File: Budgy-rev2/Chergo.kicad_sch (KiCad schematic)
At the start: 36 parts, among them K1 KEYSW, K10 KEYSW, K11 KEYSW, K12 KEYSW, K13 KEYSW, K14 KEYSW, K15 KEYSW, K16 KEYSW, K17 KEYSW, K2 KEYSW, K3 KEYSW, K4 KEYSW, K5 KEYSW, K6 KEYSW, K7 KEYSW, K8 KEYSW, K9 KEYSW, U1 Pico, U2 TRRS

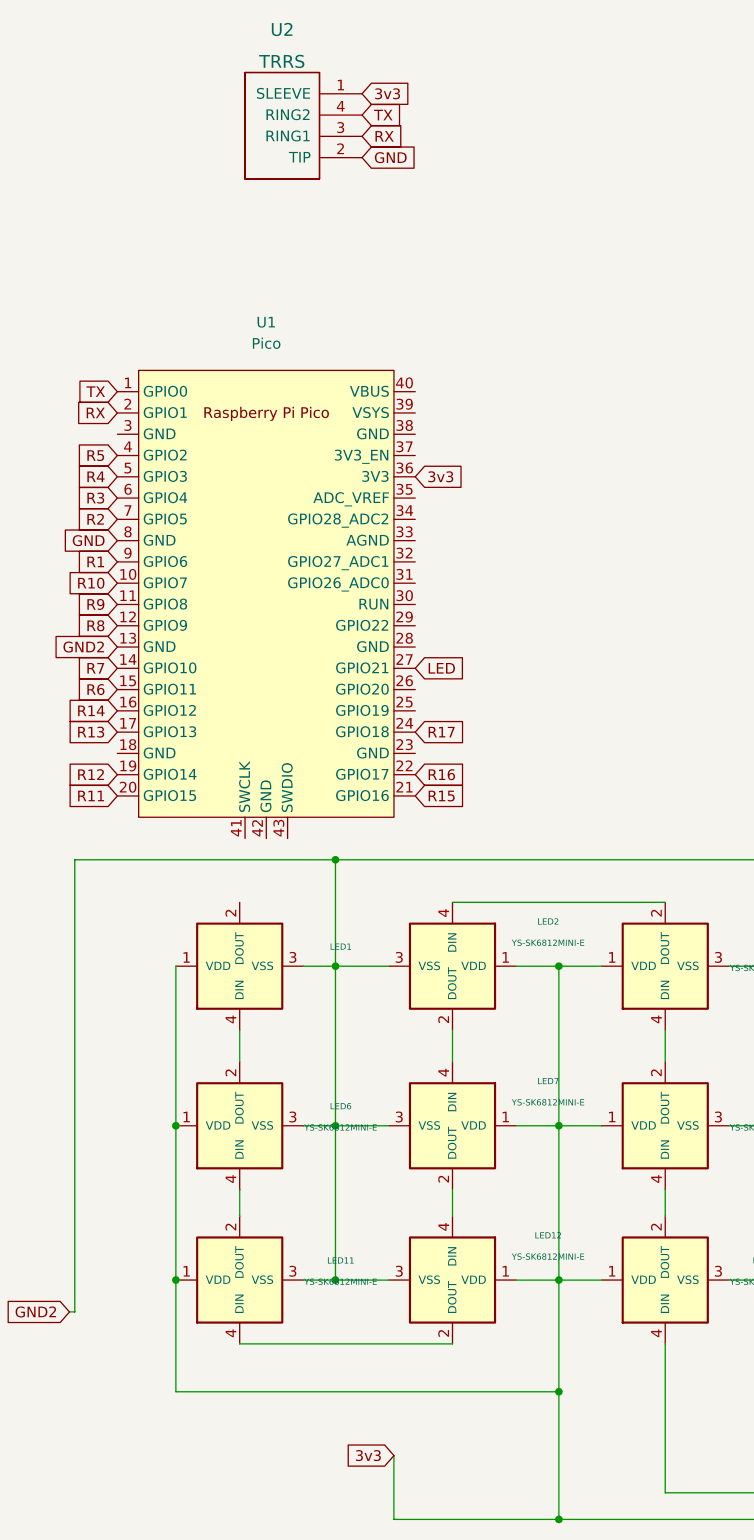
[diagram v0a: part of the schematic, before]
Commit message: changed to 5v for rgbled
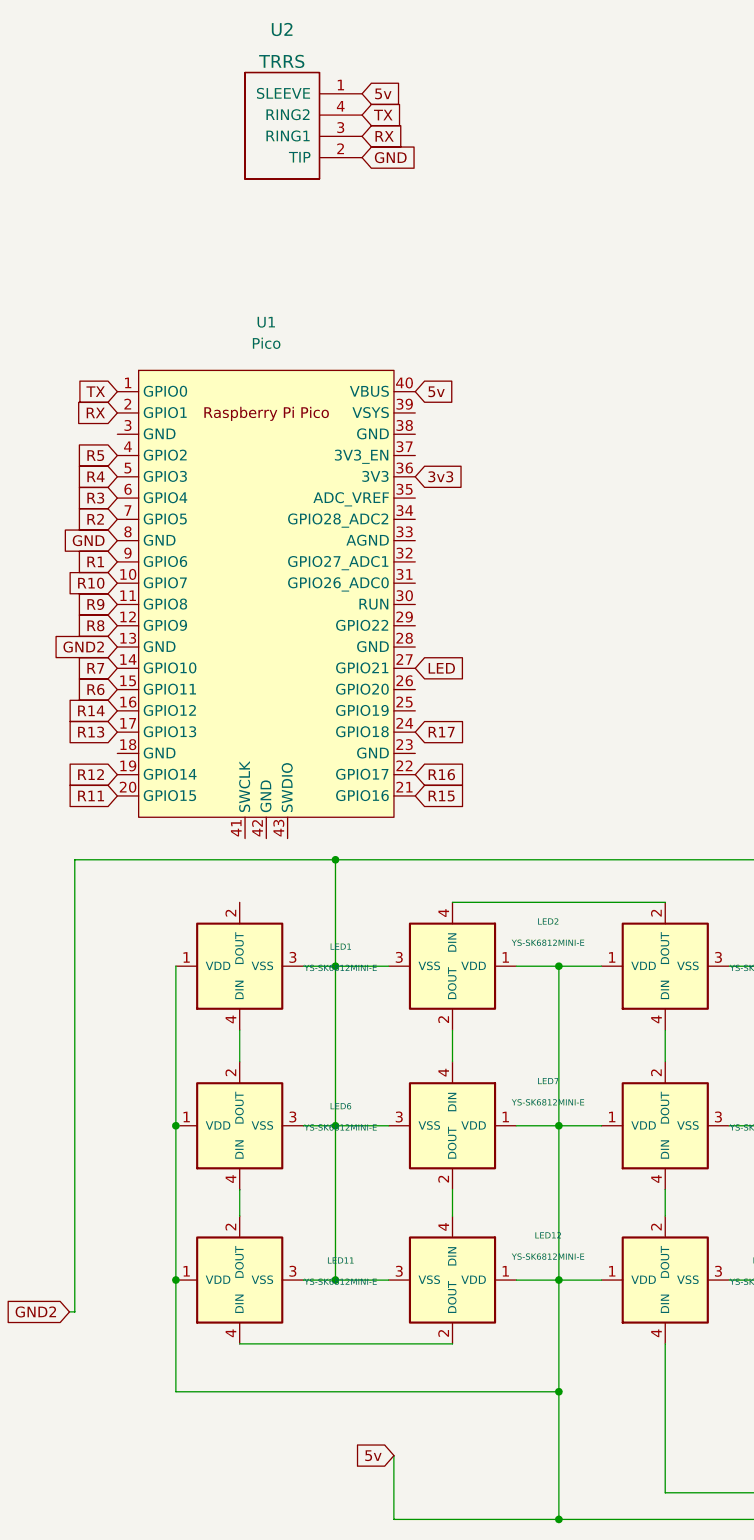
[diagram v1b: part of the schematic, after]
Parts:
- LED1: value (none) -> YS-SK6812MINI-E; footprint (none) -> kbd:YS-SK6812MINI-E-reversible-fix
- LED10, LED11, LED12, LED13, LED14, LED15, LED16, LED17, LED2, LED3, LED4, LED5, LED6, LED7, LED8, LED9: footprint (none) -> kbd:YS-SK6812MINI-E-reversible-fix
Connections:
- net 3v3: no longer LED1.1 (VDD), LED10.1 (VDD), LED11.1 (VDD), LED12.1 (VDD), LED13.1 (VDD), LED14.1 (VDD), LED15.1 (VDD), LED16.1 (VDD), LED17.1 (VDD), LED2.1 (VDD), LED3.1 (VDD), LED4.1 (VDD), LED5.1 (VDD), LED6.1 (VDD), LED7.1 (VDD), LED8.1 (VDD), LED9.1 (VDD), U2.1 (SLEEVE)
- net 5v: now reaches U1.40 (VBUS)
- net 5v: now also LED1.1 (VDD), LED10.1 (VDD), LED11.1 (VDD), LED12.1 (VDD), LED13.1 (VDD), LED14.1 (VDD), LED15.1 (VDD), LED16.1 (VDD), LED17.1 (VDD), LED2.1 (VDD), LED3.1 (VDD), LED4.1 (VDD), LED5.1 (VDD), LED6.1 (VDD), LED7.1 (VDD), LED8.1 (VDD), LED9.1 (VDD), U2.1 (SLEEVE)
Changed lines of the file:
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@@
     (stroke (width 0) (type default) (color 0 0 0 0))
   )
-  (global_label "3v3" (shape input) (at 55.245 23.495 0) (fields_autoplaced)
-    (effects (font (size 1.27 1.27)) (justify left))
-    (property "Intersheet References" "${INTERSHEET_REFS}" (id 0) (at 61.0448 23.4156 0)
-      (effects (font (size 1.27 1.27)) (justify left) hide)
-    )
-  )
   (global_label "R14" (shape input) (at 26.035 97.155 180) (fields_autoplaced)
     (effects (font (size 1.27 1.27)) (justify right))
@@
     )
   )
+  (global_label "5v" (shape input) (at 59.055 186.055 180) (fields_autoplaced)
+    (effects (font (size 1.27 1.27)) (justify right))
+    (property "Intersheet References" "${INTERSHEET_REFS}" (id 0) (at 54.4648 186.1344 0)
+      (effects (font (size 1.27 1.27)) (justify right) hide)
+    )
+  )
   (global_label "R10" (shape input) (at 245.745 61.595 180) (fields_autoplaced)
     (effects (font (size 1.27 1.27)) (justify right))
@@
     )
   )
+  (global_label "5v" (shape input) (at 61.595 59.055 0) (fields_autoplaced)
+    (effects (font (size 1.27 1.27)) (justify left))
+    (property "Intersheet References" "${INTERSHEET_REFS}" (id 0) (at 66.1852 58.9756 0)
+      (effects (font (size 1.27 1.27)) (justify left) hide)
+    )
+  )
   (global_label "R2" (shape input) (at 175.26 45.72 180) (fields_autoplaced)
     (effects (font (size 1.27 1.27)) (justify right))
@@
     )
   )
+  (global_label "5v" (shape input) (at 55.245 23.495 0) (fields_autoplaced)
+    (effects (font (size 1.27 1.27)) (justify left))
+    (property "Intersheet References" "${INTERSHEET_REFS}" (id 0) (at 59.8352 23.4156 0)
+      (effects (font (size 1.27 1.27)) (justify left) hide)
+    )
+  )
   (global_label "R9" (shape input) (at 26.035 84.455 180) (fields_autoplaced)
     (effects (font (size 1.27 1.27)) (justify right))
@@
     )
   )
-  (global_label "3v3" (shape input) (at 59.055 186.055 180) (fields_autoplaced)
-    (effects (font (size 1.27 1.27)) (justify right))
-    (property "Intersheet References" "${INTERSHEET_REFS}" (id 0) (at 53.2552 185.9756 0)
-      (effects (font (size 1.27 1.27)) (justify right) hide)
-    )
-  )
   (global_label "R6" (shape input) (at 151.765 61.595 180) (fields_autoplaced)
     (effects (font (size 1.27 1.27)) (justify right))
@@
       (effects (font (size 0.7366 0.7366)))
     )
-    (property "Footprint" "" (id 2) (at 46.99 162.56 0)
+    (property "Footprint" "kbd:YS-SK6812MINI-E-reversible-fix" (id 2) (at 46.99 162.56 0)
       (effects (font (size 1.27 1.27)) hide)
     )
@@
       (effects (font (size 0.7366 0.7366)))
     )
-    (property "Footprint" "" (id 2) (at 110.49 167.64 0)
+    (property "Footprint" "kbd:YS-SK6812MINI-E-reversible-fix" (id 2) (at 110.49 167.64 0)
       (effects (font (size 1.27 1.27)) hide)
     )
@@
       (effects (font (size 0.7366 0.7366)))
     )
-    (property "Footprint" "" (id 2) (at 148.59 162.56 0)
+    (property "Footprint" "kbd:YS-SK6812MINI-E-reversible-fix" (id 2) (at 148.59 162.56 0)
       (effects (font (size 1.27 1.27)) hide)
     )
@@
       (effects (font (size 0.7366 0.7366)))
     )
-    (property "Footprint" "" (id 2) (at 46.99 144.145 0)
+    (property "Footprint" "kbd:YS-SK6812MINI-E-reversible-fix" (id 2) (at 46.99 144.145 0)
       (effects (font (size 1.27 1.27)) hide)
     )
@@
       (effects (font (size 0.7366 0.7366)))
     )
-    (property "Footprint" "" (id 2) (at 97.79 125.095 0)
+    (property "Footprint" "kbd:YS-SK6812MINI-E-reversible-fix" (id 2) (at 97.79 125.095 0)
       (effects (font (size 1.27 1.27)) hide)
     )
@@
       (effects (font (size 0.7366 0.7366)))
     )
-    (property "Footprint" "" (id 2) (at 110.49 185.42 0)
+    (property "Footprint" "kbd:YS-SK6812MINI-E-reversible-fix" (id 2) (at 110.49 185.42 0)
       (effects (font (size 1.27 1.27)) hide)
     )
@@
       (effects (font (size 0.7366 0.7366)))
     )
-    (property "Footprint" "" (id 2) (at 148.59 180.34 0)
+    (property "Footprint" "kbd:YS-SK6812MINI-E-reversible-fix" (id 2) (at 148.59 180.34 0)
       (effects (font (size 1.27 1.27)) hide)
     )
@@
       (effects (font (size 0.7366 0.7366)))
     )
-    (property "Footprint" "" (id 2) (at 148.59 125.095 0)
+    (property "Footprint" "kbd:YS-SK6812MINI-E-reversible-fix" (id 2) (at 148.59 125.095 0)
       (effects (font (size 1.27 1.27)) hide)
     )
@@
       (effects (font (size 0.7366 0.7366)))
     )
-    (property "Footprint" "" (id 2) (at 110.49 130.175 0)
+    (property "Footprint" "kbd:YS-SK6812MINI-E-reversible-fix" (id 2) (at 110.49 130.175 0)
       (effects (font (size 1.27 1.27)) hide)
     )
@@
       (effects (font (size 0.7366 0.7366)))
     )
-    (property "Value" "" (id 1) (at 52.705 127.8636 90)
-      (effects (font (size 0.7366 0.7366)))
-    )
-    (property "Footprint" "" (id 2) (at 46.99 125.095 0)
+    (property "Value" "YS-SK6812MINI-E" (id 1) (at 52.705 127.8636 90)
+      (effects (font (size 0.7366 0.7366)))
+    )
+    (property "Footprint" "kbd:YS-SK6812MINI-E-reversible-fix" (id 2) (at 46.99 125.095 0)
       (effects (font (size 1.27 1.27)) hide)
     )
@@
       (effects (font (size 0.7366 0.7366)))
     )
-    (property "Footprint" "" (id 2) (at 97.79 144.145 0)
+    (property "Footprint" "kbd:YS-SK6812MINI-E-reversible-fix" (id 2) (at 97.79 144.145 0)
       (effects (font (size 1.27 1.27)) hide)
     )
@@
       (effects (font (size 0.7366 0.7366)))
     )
-    (property "Footprint" "" (id 2) (at 148.59 144.145 0)
+    (property "Footprint" "kbd:YS-SK6812MINI-E-reversible-fix" (id 2) (at 148.59 144.145 0)
       (effects (font (size 1.27 1.27)) hide)
     )
@@
       (effects (font (size 0.7366 0.7366)))
     )
-    (property "Footprint" "" (id 2) (at 59.69 149.225 0)
+    (property "Footprint" "kbd:YS-SK6812MINI-E-reversible-fix" (id 2) (at 59.69 149.225 0)
       (effects (font (size 1.27 1.27)) hide)
     )
@@
       (effects (font (size 0.7366 0.7366)))
     )
-    (property "Footprint" "" (id 2) (at 59.69 130.175 0)
+    (property "Footprint" "kbd:YS-SK6812MINI-E-reversible-fix" (id 2) (at 59.69 130.175 0)
       (effects (font (size 1.27 1.27)) hide)
     )
@@
       (effects (font (size 0.7366 0.7366)))
     )
-    (property "Footprint" "" (id 2) (at 59.69 167.64 0)
+    (property "Footprint" "kbd:YS-SK6812MINI-E-reversible-fix" (id 2) (at 59.69 167.64 0)
       (effects (font (size 1.27 1.27)) hide)
     )
@@
       (effects (font (size 0.7366 0.7366)))
     )
-    (property "Footprint" "" (id 2) (at 97.79 162.56 0)
+    (property "Footprint" "kbd:YS-SK6812MINI-E-reversible-fix" (id 2) (at 97.79 162.56 0)
       (effects (font (size 1.27 1.27)) hide)
     )
@@
       (effects (font (size 0.7366 0.7366)))
     )
-    (property "Footprint" "" (id 2) (at 110.49 149.225 0)
-      (effects (font (size 1.27 1.27)) hide)
-    )
+    (property "Footprint" "kbd:YS-SK6812MINI-E-reversible-fix" (id 2) (at 110.49 149.225 0)
+      (effects (font (size 1.27 1.27)) hide)
+    )

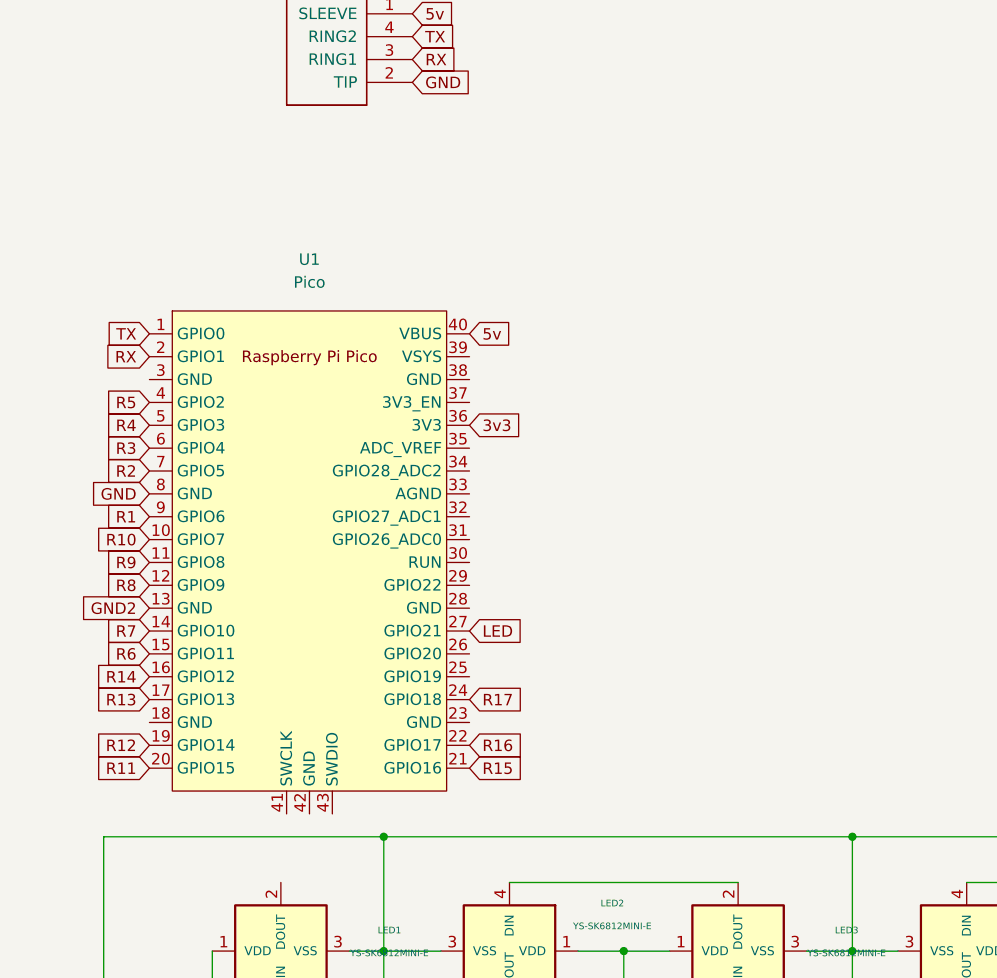
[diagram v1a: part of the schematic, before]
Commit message: add voltage divider
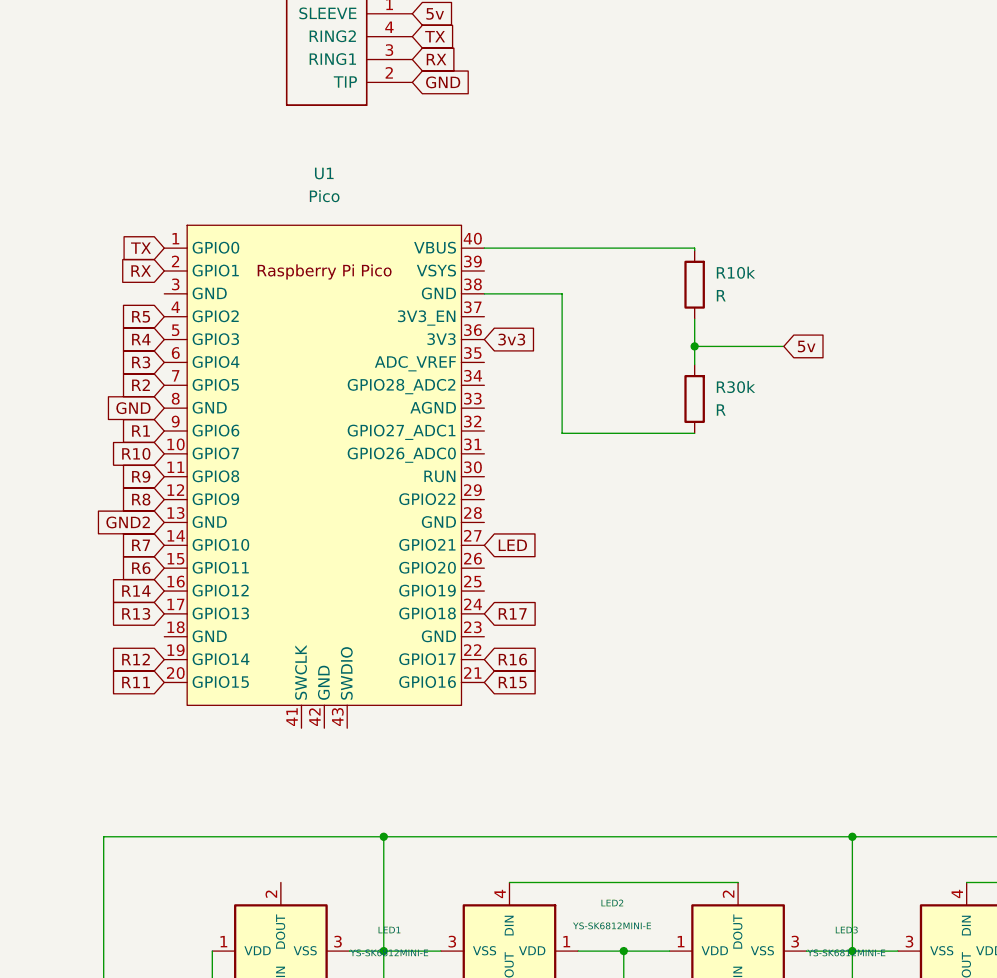
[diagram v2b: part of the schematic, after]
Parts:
- added R10k, R30k: R, kbd:R, symbol Device:R
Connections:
- net 5v: now also R10k.1, R30k.2; no longer U1.40 (VBUS)
- net at U1.38 (GND): now also R30k.1
- new net: R10k.2, U1.40 (VBUS)
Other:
- moved on the sheet: U1

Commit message: updates to rev2
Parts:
- removed R10k, R30k: R, kbd:R, symbol Device:R
- added U3: (no value), symbol Logic_LevelTranslator:SN74LVC1T45DCK
- added U4: SN74LVC1T45DCK, Keebio-Parts:SOT-363_SC-70-6, symbol Logic_LevelTranslator:SN74LVC1T45DCK
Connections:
- net 3v3: now also U2.1 (SLEEVE), U3.1 (VCCA), U3.5 (DIR), U4.1 (VCCA), U4.5 (DIR)
- net 5v: now also U1.40 (VBUS), U3.6 (VCCB), U4.6 (VCCB); no longer U2.1 (SLEEVE)
- net LED renamed LED3V
- net LED3V: now also U3.3 (A), U4.3 (A); no longer LED17.4 (DIN)
- new net GND3: U3.2 (GND), U4.2 (GND)
- new net LED5V: LED17.4 (DIN), U3.4 (B), U4.4 (B)
